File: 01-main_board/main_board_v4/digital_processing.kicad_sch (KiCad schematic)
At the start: 28 parts, among them IC9 LSF0108PWR, T1 749013011

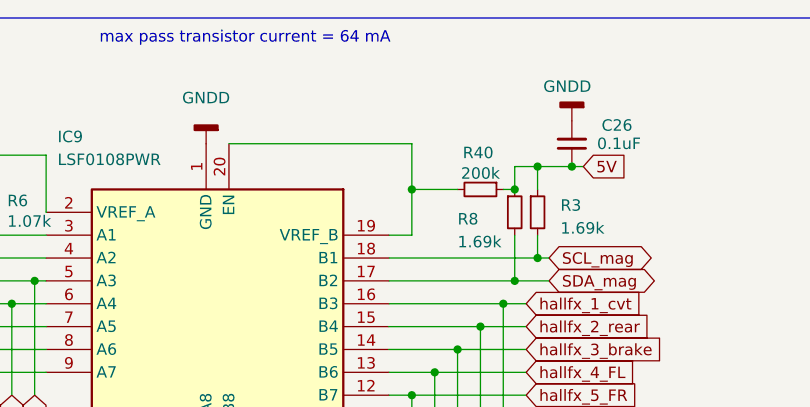
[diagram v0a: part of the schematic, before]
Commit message: Added comments and a resistor change
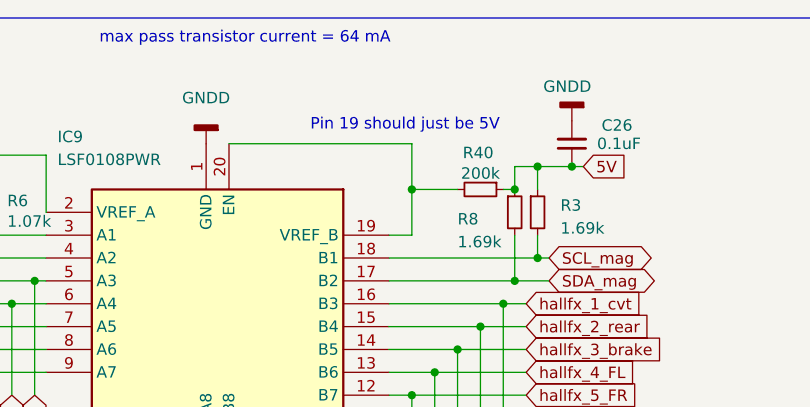
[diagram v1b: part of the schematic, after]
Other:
- note added: "Pin 19 should just be 5V"
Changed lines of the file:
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@@
+		)
+	)
+	(text "Pin 19 should just be 5V"
+		(exclude_from_sim no)
+		(at 145.288 38.608 0)
+		(effects
+			(font
+				(size 1.27 1.27)
+			)
 		)
 	)
